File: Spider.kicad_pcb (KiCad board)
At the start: 2 copper layers, 165 x 35 mm, 47 parts, among them J1 Conn_02x20_Odd_Even, J2 USB_B_Micro, SW1 SW_DPDT_x2, SW2 SW_DPDT_x2, SW3 SW_DPDT_x2, SW4 SW_DPDT_x2, SW5 SW_DPDT_x2, SW6 SW_DPDT_x2, SW7 SW_DPDT_x2, SW8 SW_DPDT_x2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

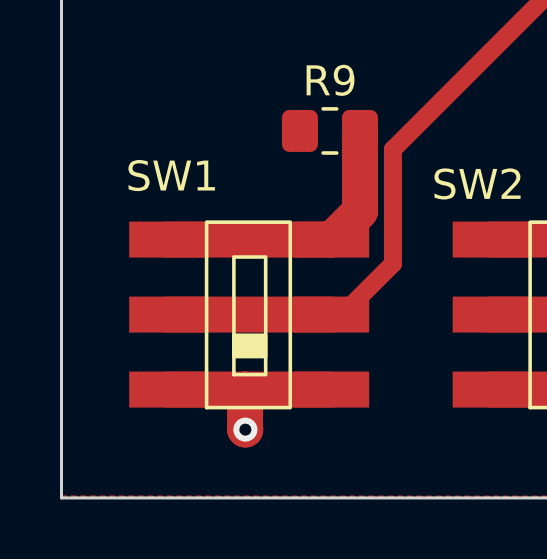
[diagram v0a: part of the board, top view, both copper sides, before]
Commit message: 1-0 mark on silkscreen
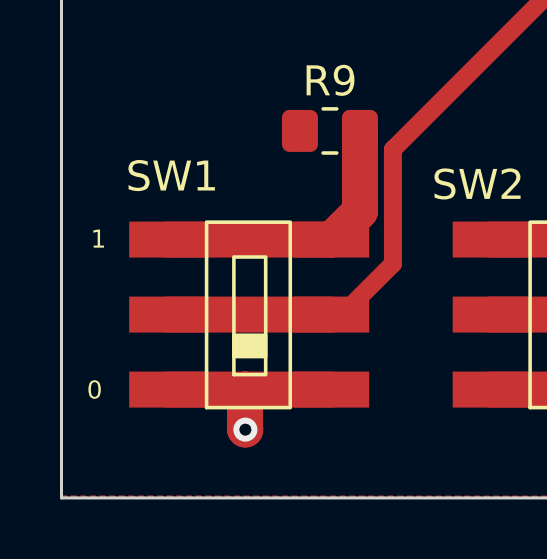
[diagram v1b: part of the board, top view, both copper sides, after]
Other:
- board text added: "0"
- board text added: "1"
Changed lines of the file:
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@@
+    (effects (font (size 0.6 0.6) (thickness 0.12)))
+  )
+  (gr_text "0" (at 51.1048 81.407) (layer "F.SilkS")
     (effects (font (size 0.6 0.6) (thickness 0.12)))
   )
@@
     (effects (font (size 0.6 0.6) (thickness 0.12)))
   )
+  (gr_text "1" (at 51.2318 76.3778) (layer "F.SilkS")
+    (effects (font (size 0.6 0.6) (thickness 0.12)))
+  )

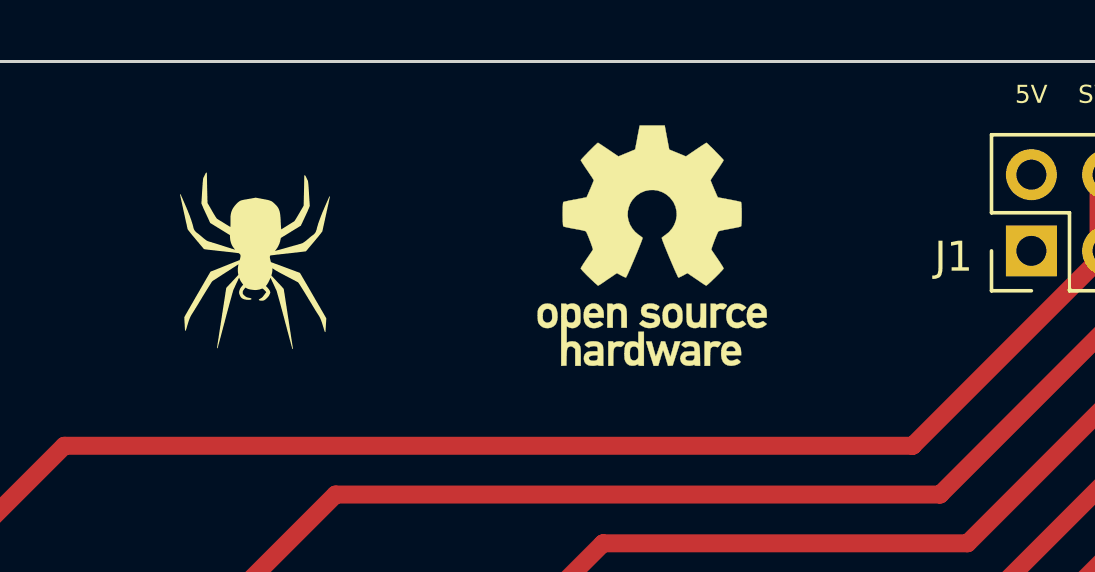
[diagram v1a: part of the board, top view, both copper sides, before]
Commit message: url of project to silkscreen
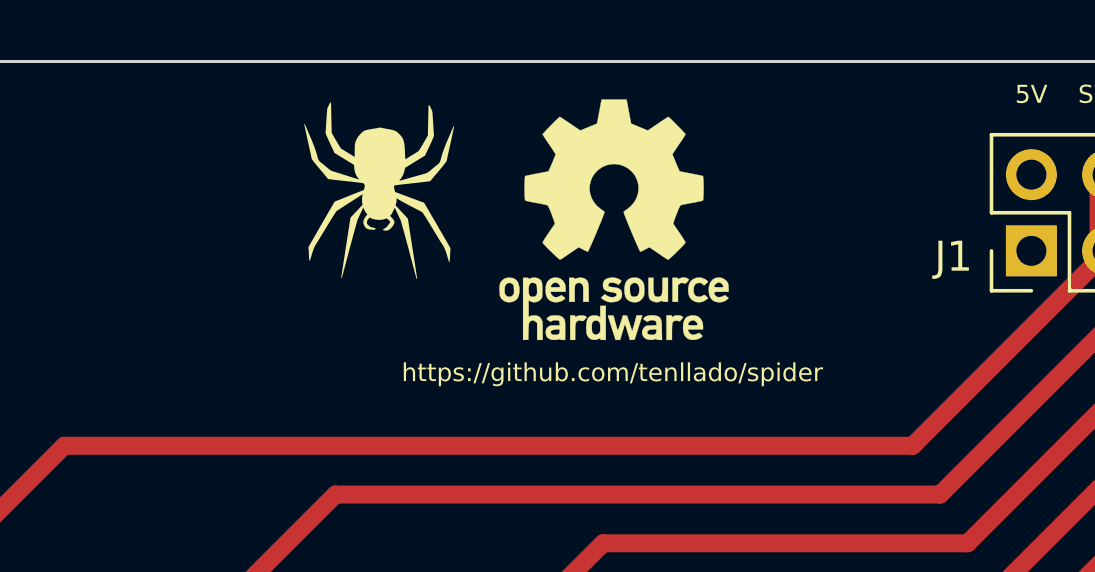
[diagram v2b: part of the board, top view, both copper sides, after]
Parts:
- moved LOGO3 4.75 mm to (82.1, 54.3)
- moved LOGO2 1.54 mm to (89.9, 55.3)
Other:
- board text added: "https://github.com/tenllado/spider"
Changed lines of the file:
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@@
   )
   (footprint "spider:spider_logo" (layer "F.Cu")
-    (at 77.978 56.642)
+    (at 82.1182 54.3052)
     (property "Sheetfile" "Spider.kicad_sch")
     (property "Sheetname" "")
@@
   )
   (footprint "Symbol:OSHW-Logo_7.5x8mm_SilkScreen" (layer "F.Cu")
-    (at 91.2114 56.134)
+    (at 89.9414 55.2704)
     (descr "Open Source Hardware Logo")
     (tags "Logo OSHW")
@@
     (effects (font (size 0.6 0.6) (thickness 0.12)))
   )
+  (gr_text "https://github.com/tenllado/spider" (at 89.8906 60.3758) (layer "F.SilkS")
+    (effects (font (size 0.6 0.6) (thickness 0.12)))
+  )

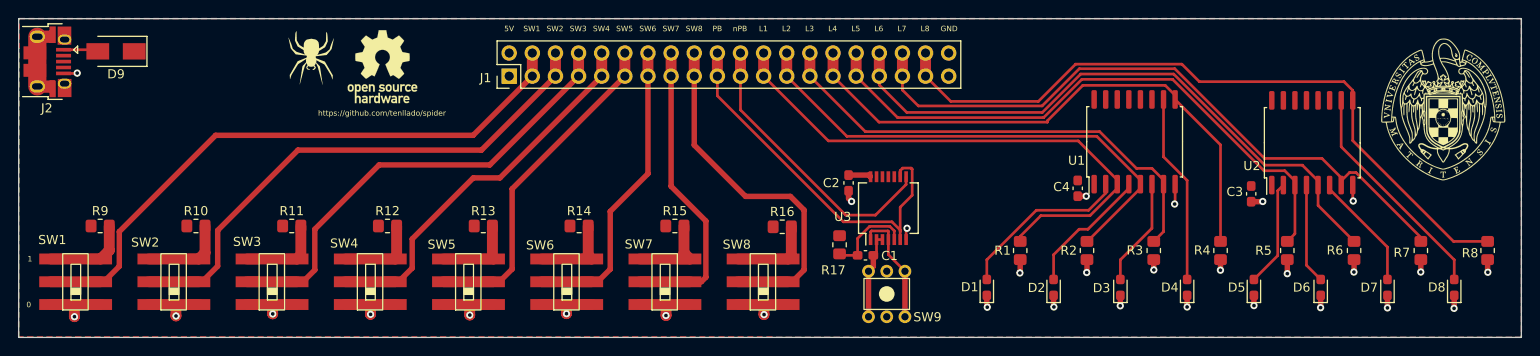
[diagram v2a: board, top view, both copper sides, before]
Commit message: split inputs and outputs, mounting holes, smd sockets
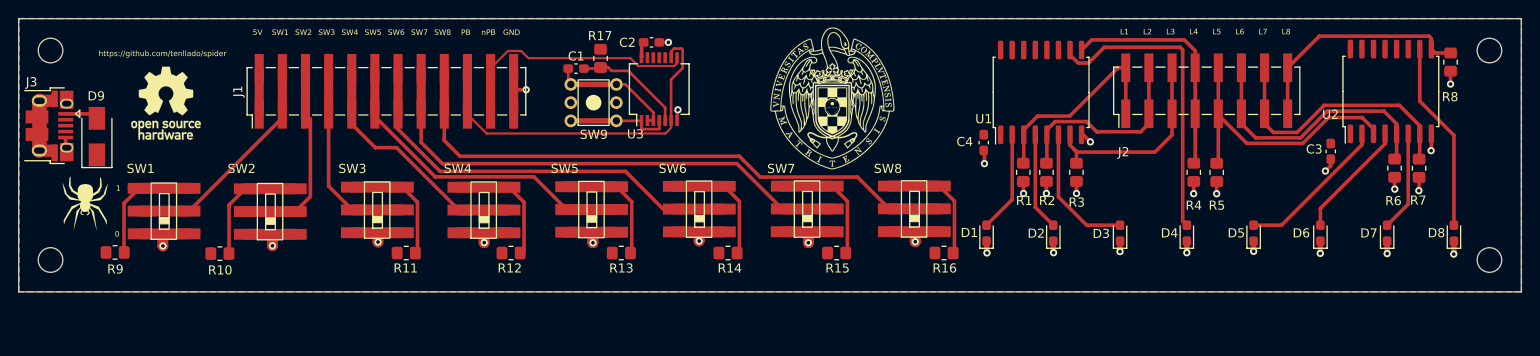
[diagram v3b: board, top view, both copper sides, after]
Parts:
- added H1: MountingHole, MountingHole:MountingHole_2.7mm_M2.5, F.Cu at (53.5, 53.5)
- added H2: MountingHole, MountingHole:MountingHole_2.7mm_M2.5, F.Cu at (53.5, 76.5)
- added H3: MountingHole, MountingHole:MountingHole_2.7mm_M2.5, F.Cu at (211.5, 53.5)
- added H4: MountingHole, MountingHole:MountingHole_2.7mm_M2.5, F.Cu at (211.5, 76.5)
- added J3: USB_B_Micro, Connector_USB:USB_Micro-B_Amphenol_10103594-0001LF_Horizontal, F.Cu at (53.4, 61.8)
- J1: value Conn_02x20_Odd_Even -> Conn_02x12_Odd_Even; footprint Connector_PinHeader_2.54mm:PinHeader_2x20_P2.54mm_Vertical -> Connector_PinHeader_2.54mm:PinHeader_2x12_P2.54mm_Vertical_SMD
- J2: value USB_B_Micro -> Conn_02x08_Odd_Even; footprint Connector_USB:USB_Micro-B_Amphenol_10103594-0001LF_Horizontal -> Connector_PinHeader_2.54mm:PinHeader_2x08_P2.54mm_Vertical_SMD
- moved J2 127.3 mm to (180.5, 57.9), turned to 90 degrees
- moved LOGO1 67.1 mm to (139.5, 59.0)
- moved SW9 38.4 mm to (113.1, 59.2), turned to 90 degrees
- moved C1 37.8 mm to (111.2, 55.5), turned to 0 degrees
- moved R17 33.3 mm to (113.9, 54.4)
- moved LOGO3 29.5 mm to (57.3, 70.2)
- moved U3 28.4 mm to (120.3, 57.7)
- moved C2 26.6 mm to (119.5, 52.6), turned to 0 degrees
- moved LOGO2 24.1 mm to (66.2, 59.3)
- moved R8 21.1 mm to (207.2, 54.8)
- moved SW8 18.4 mm to (148.4, 70.9)
- moved R15 18.0 mm to (139.8, 75.7)
- moved R16 18.0 mm to (151.6, 75.7)
- moved SW7 17.6 mm to (136.6, 70.9)
- moved R14 16.6 mm to (127.9, 75.7)
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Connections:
- J1 pad 23: /LED1 -> GND
- J1 pad 24: /LED1 -> GND
- J2 pad 1: Net-(D9-Pad2) -> /LED1
- J2 pad 2: unconnected-(J2-Pad2) -> /LED1
- J2 pad 3: unconnected-(J2-Pad3) -> /LED2
- J2 pad 4: unconnected-(J2-Pad4) -> /LED2
- J2 pad 5: GND -> /LED3
- J2 pad 6: GND -> /LED3
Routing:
- net /LED8: track 78.4 -> 25.8 mm
- net /LED7: track 73.4 -> 29.4 mm
- net /SW1: track 67.0 -> 25.4 mm
- net /LED6: track 67.8 -> 29.6 mm
- net /LED1: track 60.4 -> 22.8 mm
- net /SW2: track 58.8 -> 22.1 mm
- net /LED4: track 62.5 -> 25.8 mm
- net /LED5: track 66.0 -> 31.2 mm
- net /LED2: track 55.3 -> 22.3 mm
- net /LED3: track 53.3 -> 22.4 mm
- net /SW3: track 50.9 -> 22.1 mm
- net /SW8: track 39.5 -> 65.4 mm
- net /SW7: track 33.7 -> 56.3 mm
- net /SW4: track 41.9 -> 27.3 mm
- net Net-(D4-Pad2): track 20.8 -> 33.5 mm
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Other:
- board size 165 x 35 mm -> 165 x 30 mm

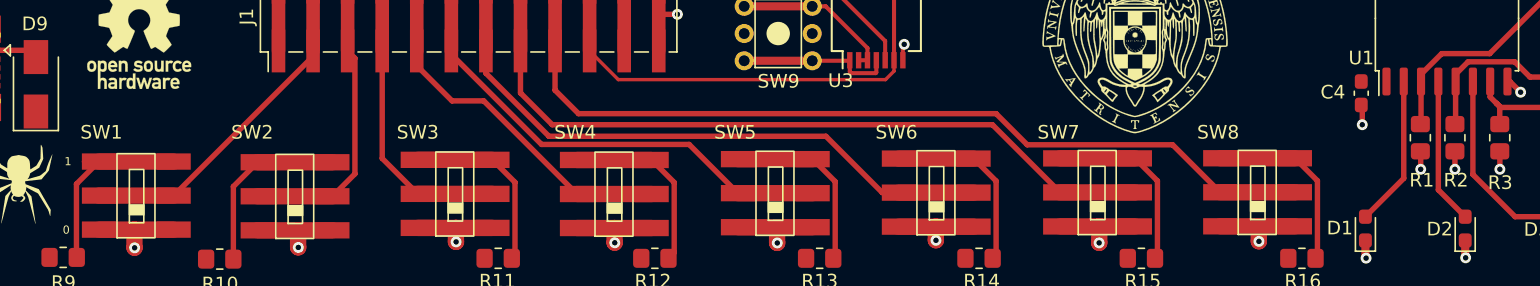
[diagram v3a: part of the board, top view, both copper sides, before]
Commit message: remove small tracks, pcb erc warnings
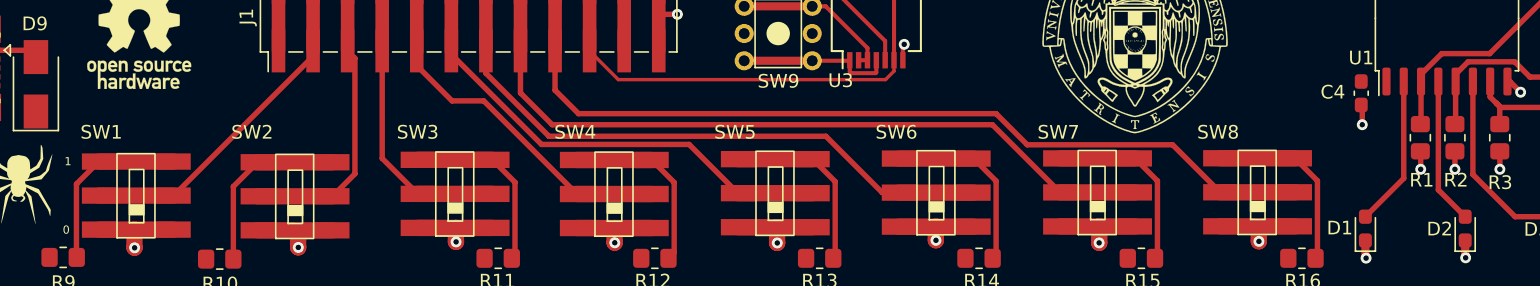
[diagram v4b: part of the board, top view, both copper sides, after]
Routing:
- net Net-(R9-Pad2): track 14.3 -> 13.2 mm
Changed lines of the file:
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@@
   (segment (start 121.977051 55.20746) (end 122.29 54.894511) (width 0.25) (layer "F.Cu") (net 23))
   (segment (start 117.18 54.34) (end 118.04746 55.20746) (width 0.25) (layer "F.Cu") (net 23))
-  (segment (start 160.364014 65.9099) (end 160.313214 65.9607) (width 0.4) (layer "F.Cu") (net 24))
   (segment (start 171.565414 55.3933) (end 170.712214 55.3933) (width 0.4) (layer "F.Cu") (net 24))
   (segment (start 171.565414 55.3933) (end 171.565414 60.4433) (width 0.4) (layer "F.Cu") (net 24))
@@
   (segment (start 160.364014 62.7461) (end 160.364014 65.9099) (width 0.4) (layer "F.Cu") (net 24))
   (segment (start 165.408534 60.69698) (end 161.880996 60.69698) (width 0.4) (layer "F.Cu") (net 24))
-  (segment (start 162.904014 65.8845) (end 162.853214 65.9353) (width 0.4) (layer "F.Cu") (net 25))
   (segment (start 163.821476 61.2965) (end 162.904014 62.213962) (width 0.4) (layer "F.Cu") (net 25))
   (segment (start 173.205414 62.4183) (end 168.369214 62.4183) (width 0.4) (layer "F.Cu") (net 25))
@@
   (segment (start 192.818734 51.91998) (end 204.860894 51.91998) (width 0.4) (layer "F.Cu") (net 31))
   (segment (start 63.2178 68.6277) (end 68.7178 68.6277) (width 1.2) (layer "F.Cu") (net 32))
-  (segment (start 63.2178 68.6277) (end 62.150456 68.6277) (width 0.4) (layer "F.Cu") (net 32))
   (segment (start 61.568289 70.277211) (end 63.2178 68.6277) (width 0.4) (layer "F.Cu") (net 32))
   (segment (start 61.590528 75.6691) (end 61.568289 75.646861) (width 0.4) (layer "F.Cu") (net 32))
